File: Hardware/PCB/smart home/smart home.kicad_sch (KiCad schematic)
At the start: 51 parts, among them M1 Fan, Q1 BC547C, Q2 BC547C, Q3 BC547, Q6 BC547C, Q7 BC547C, Q8 BC547C, Q9 BC547C, SW1 SW_SPST, SW2 SW_SPST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

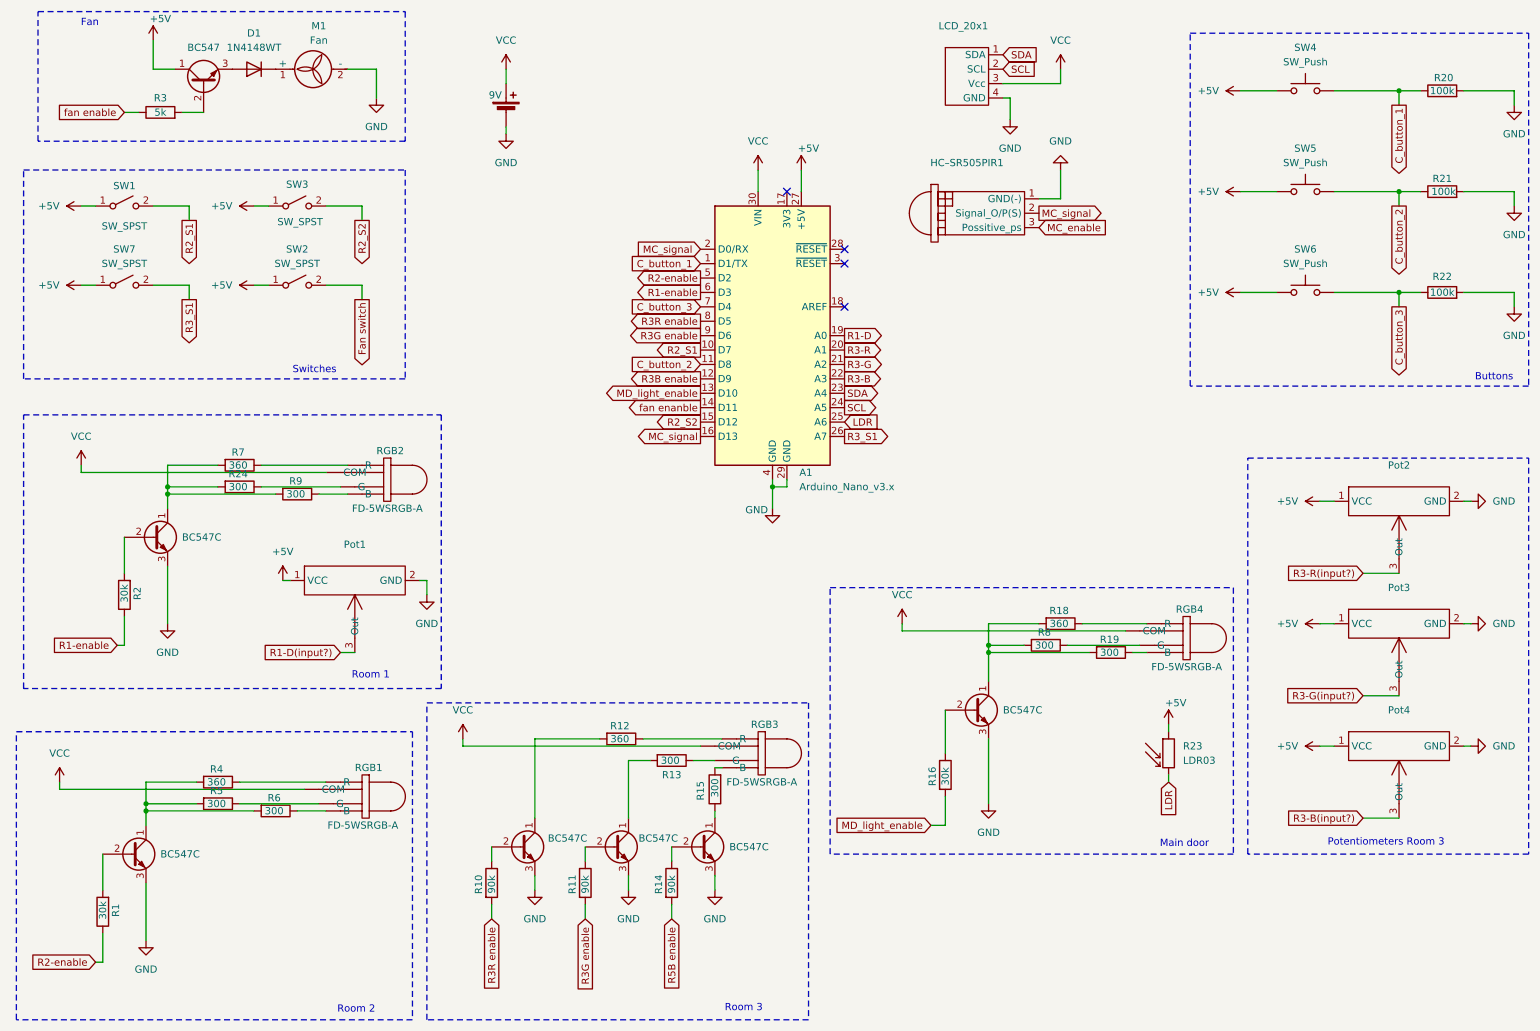
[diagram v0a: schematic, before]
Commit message: Update resistors and fan circuit
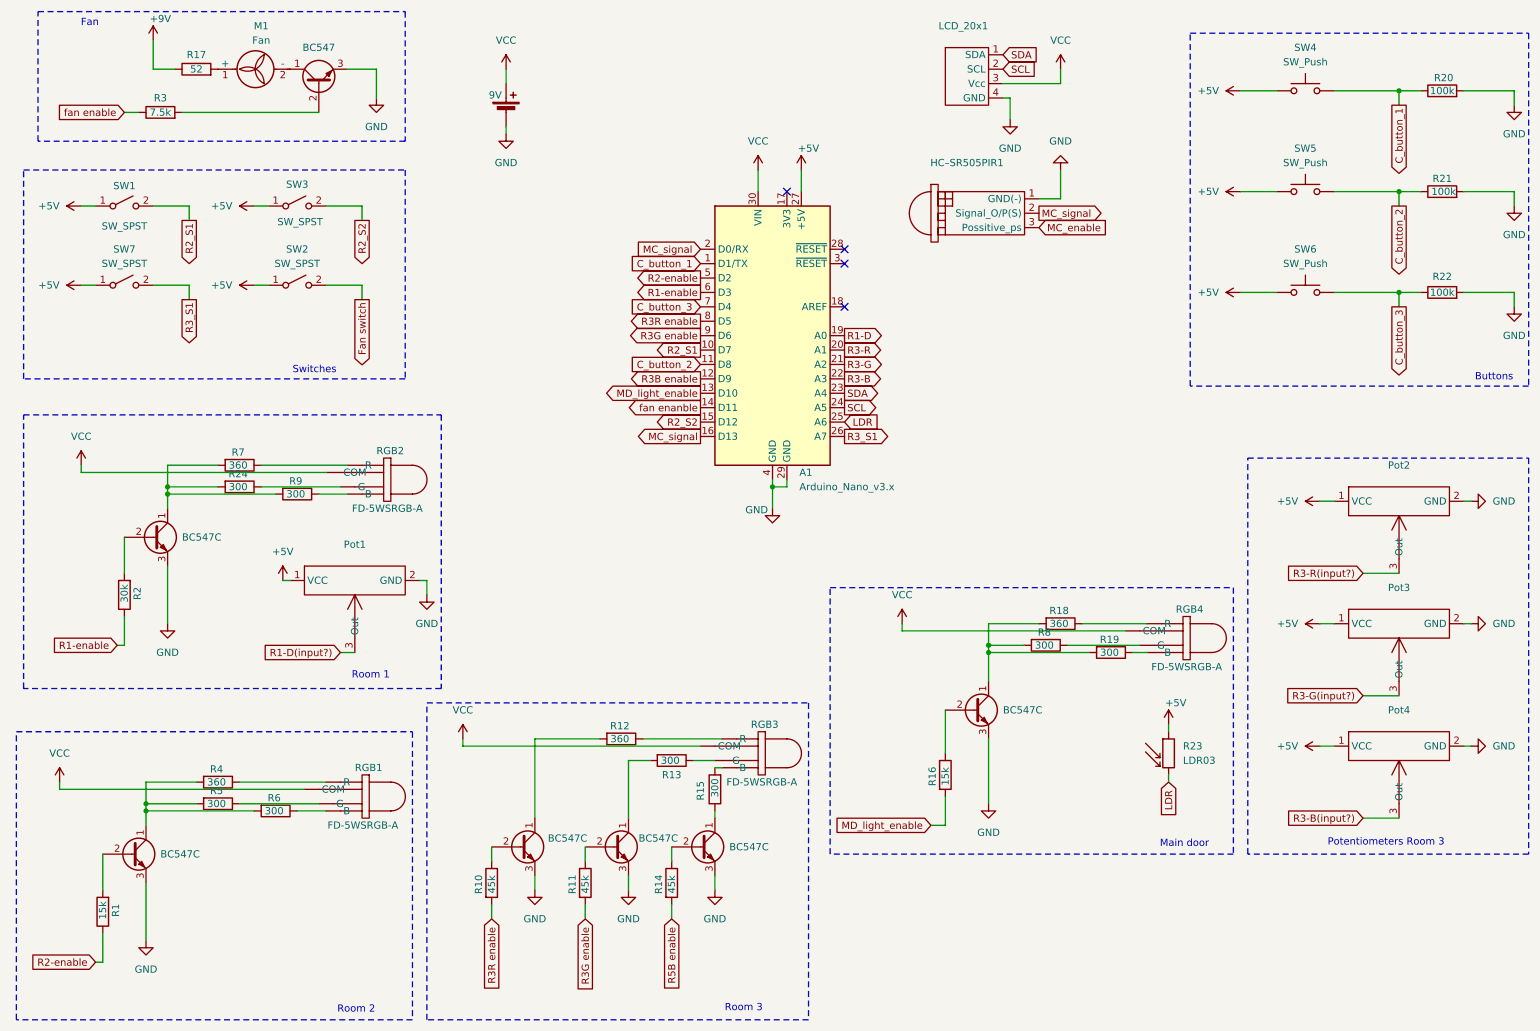
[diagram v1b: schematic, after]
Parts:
- removed D1: 1N4148WT, Diode_SMD:D_SOD-523, symbol Diode:1N4148WT
- added R17: 52, symbol Device:R
- R1, R16: value 30k -> 15k
- R10, R11, R14: value 90k -> 45k
- R3: value 5k -> 7.5k
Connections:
- net +5V: no longer Q3.1 (C)
- net GND: now also Q3.3 (E); no longer M1.2 (-)
- net at M1.1 (+): now also R17.2
- new net: M1.2 (-), Q3.1 (C)
- new net +9V: R17.1
